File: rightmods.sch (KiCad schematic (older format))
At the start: 22 parts

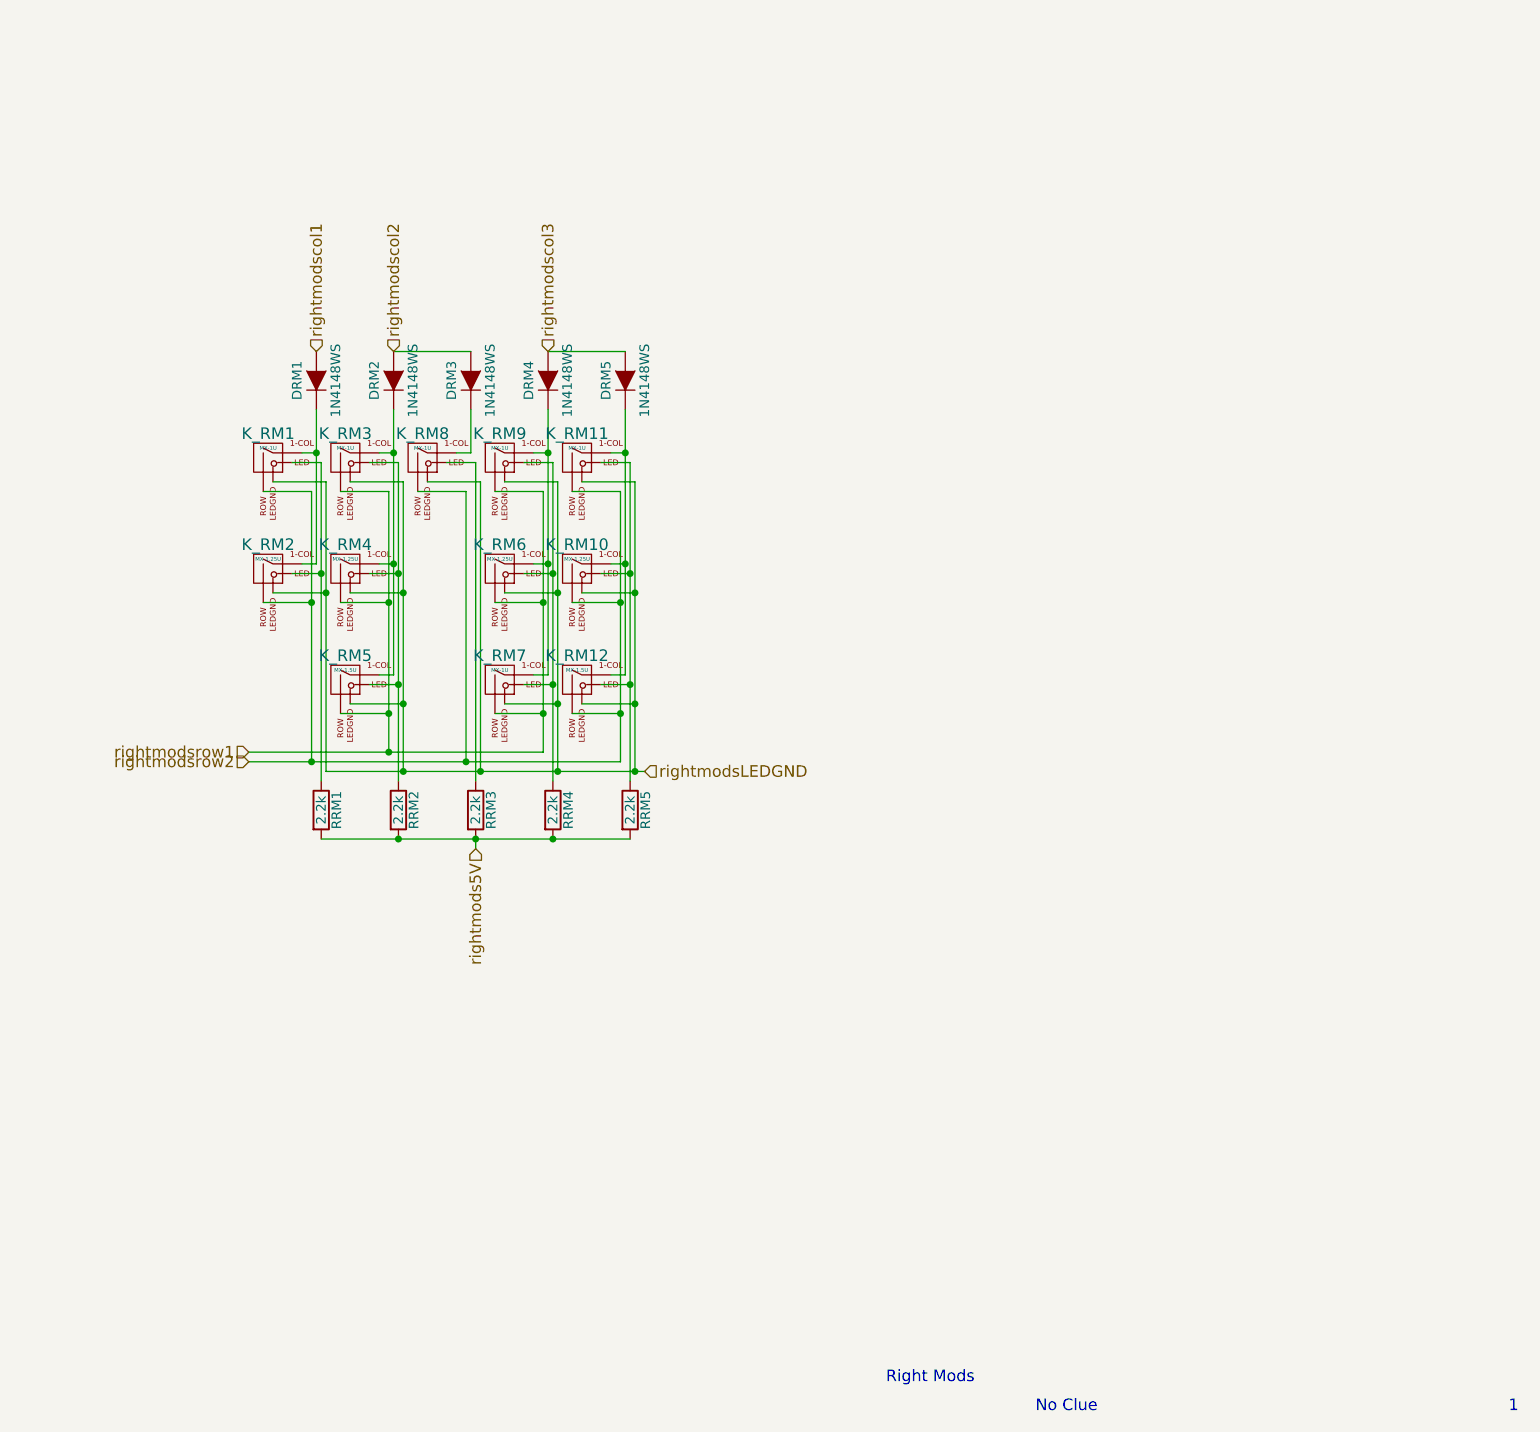
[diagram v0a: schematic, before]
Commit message: Added more right shift layouts
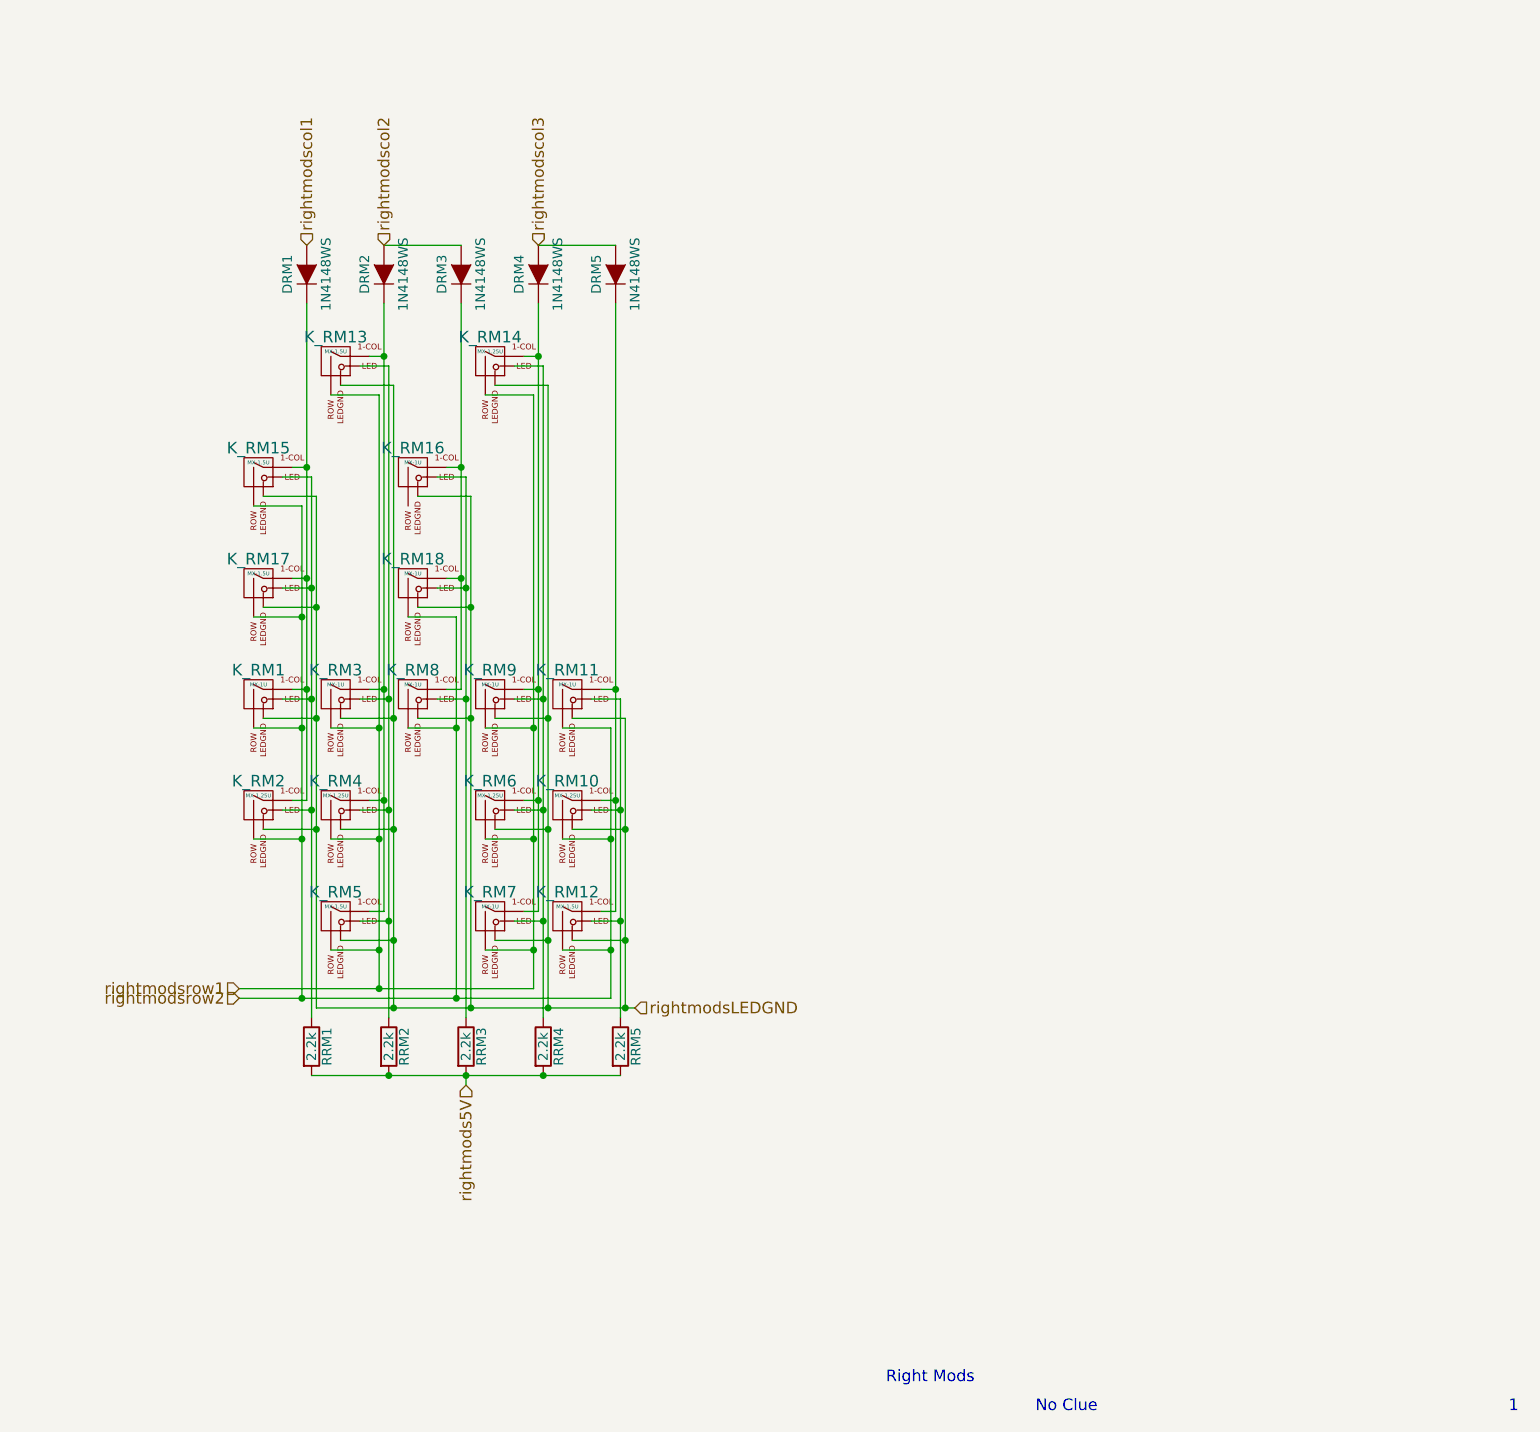
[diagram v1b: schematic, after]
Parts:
- added K_RM13, K_RM15, K_RM17: MX-1.5U, MX_Alps_Hybrid:MX-1.5U, symbol MX-1.5U
- added K_RM14: MX-1.25U, MX_Alps_Hybrid:MX-1.25U, symbol MX-1.25U
- added K_RM16, K_RM18: MX-1U, MX_Alps_Hybrid:MX-1U, symbol MX-1U
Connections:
- net rightmodsLEDGND: now also K_RM13.4 (LEDGND), K_RM14.4 (LEDGND), K_RM15.4 (LEDGND), K_RM16.4 (LEDGND), K_RM17.4 (LEDGND), K_RM18.4 (LEDGND)
- net rightmodsrow1: now also K_RM13.2 (ROW), K_RM14.2 (ROW)
- net rightmodsrow2: now also K_RM15.2 (ROW), K_RM17.2 (ROW), K_RM18.2 (ROW)
- net at DRM1.1 (K), K_RM1.1 (COL), K_RM2.1 (COL): now also K_RM15.1 (COL), K_RM17.1 (COL)
- net at K_RM1.3 (LED), K_RM2.3 (LED), RRM1.1: now also K_RM15.3 (LED), K_RM17.3 (LED)
- net at DRM2.1 (K), K_RM3.1 (COL), K_RM4.1 (COL)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: now also K_RM13.1 (COL)
- net at K_RM3.3 (LED), K_RM4.3 (LED), K_RM5.3 (LED)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: now also K_RM13.3 (LED)
- net at DRM4.1 (K), K_RM6.1 (COL), K_RM7.1 (COL)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: now also K_RM14.1 (COL)
- net at K_RM6.3 (LED), K_RM7.3 (LED), K_RM9.3 (LED)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: now also K_RM14.3 (LED)
- net at DRM3.1 (K), K_RM8.1 (COL): now also K_RM16.1 (COL), K_RM18.1 (COL)
- net at K_RM8.3 (LED), RRM3.1: now also K_RM16.3 (LED), K_RM18.3 (LED)
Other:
- moved on the sheet: DRM1, DRM2, DRM3, DRM4, DRM5, K_RM1, K_RM10, K_RM11, K_RM12, K_RM2, K_RM3, K_RM4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

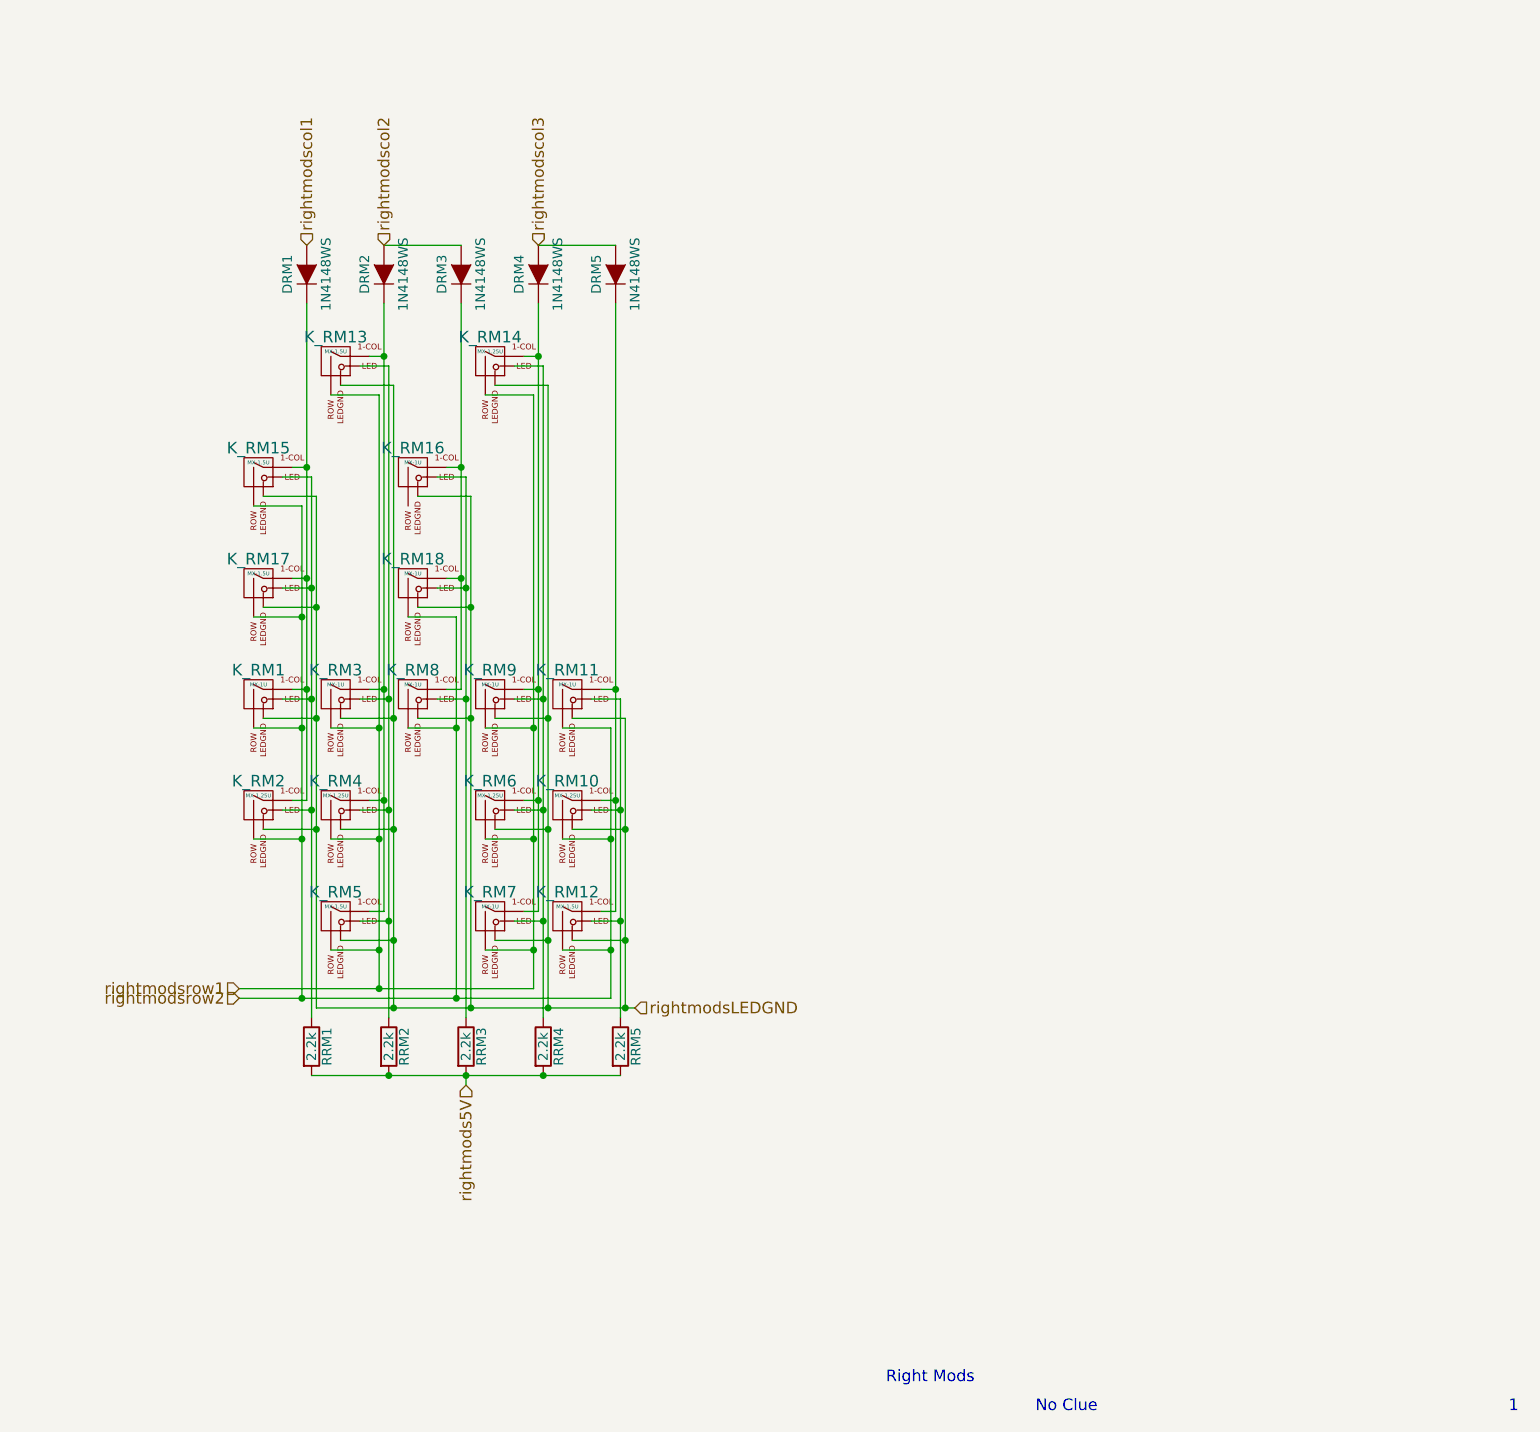
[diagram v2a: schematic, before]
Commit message: Fix RMods Diode Location
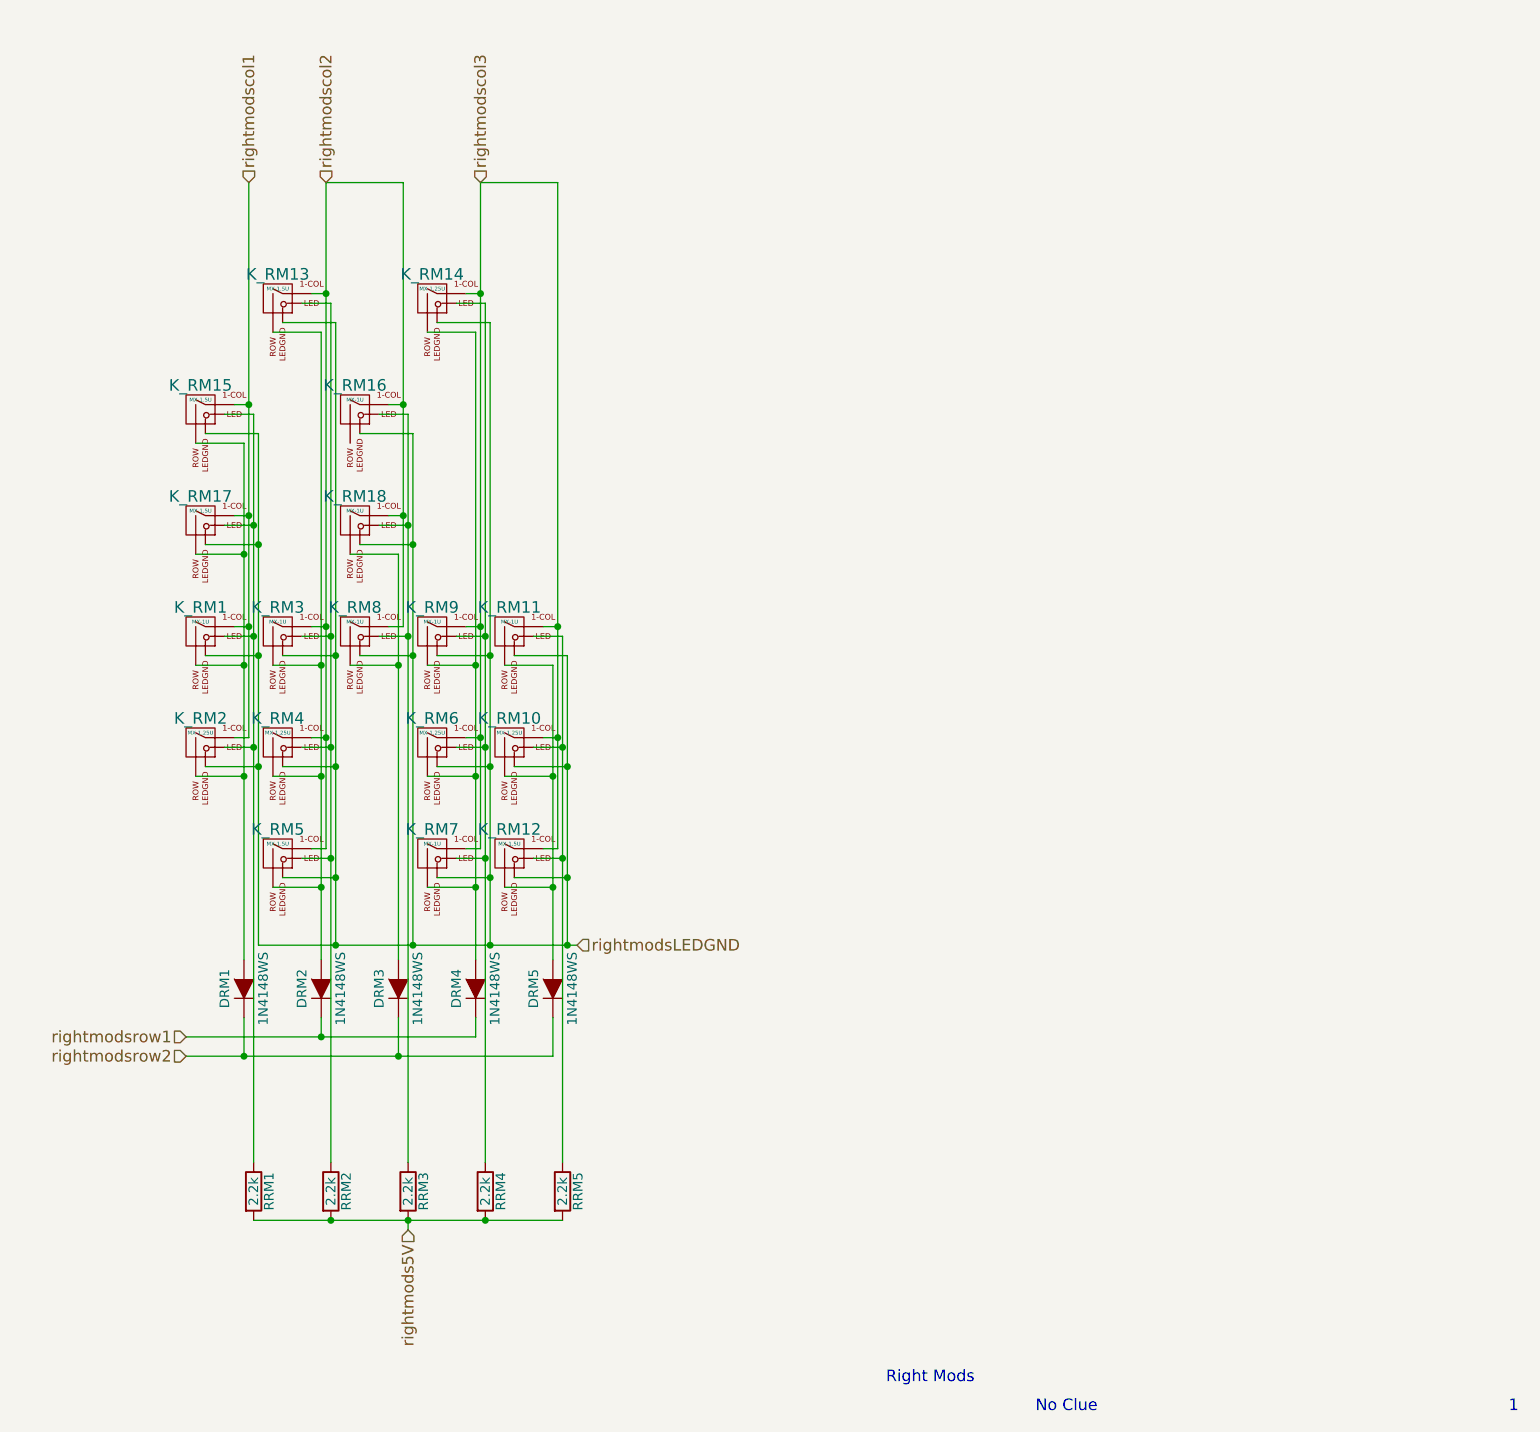
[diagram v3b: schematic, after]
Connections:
- net rightmodscol1: now also K_RM1.1 (COL), K_RM15.1 (COL), K_RM17.1 (COL), K_RM2.1 (COL); no longer DRM1.2 (A)
- net rightmodscol2: now also K_RM13.1 (COL), K_RM16.1 (COL), K_RM18.1 (COL), K_RM3.1 (COL), K_RM4.1 (COL), K_RM5.1 (COL), K_RM8.1 (COL); no longer DRM2.2 (A), DRM3.2 (A)
- net rightmodscol3: now also K_RM10.1 (COL), K_RM11.1 (COL), K_RM12.1 (COL), K_RM14.1 (COL), K_RM6.1 (COL), K_RM7.1 (COL), K_RM9.1 (COL); no longer DRM4.2 (A), DRM5.2 (A)
- net rightmodsrow1: now also DRM2.1 (K), DRM4.1 (K); no longer K_RM13.2 (ROW), K_RM14.2 (ROW), K_RM3.2 (ROW), K_RM4.2 (ROW), K_RM5.2 (ROW), K_RM6.2 (ROW), K_RM7.2 (ROW), K_RM9.2 (ROW)
- net rightmodsrow2: now also DRM1.1 (K), DRM3.1 (K), DRM5.1 (K); no longer K_RM1.2 (ROW), K_RM10.2 (ROW), K_RM11.2 (ROW), K_RM12.2 (ROW), K_RM15.2 (ROW), K_RM17.2 (ROW), K_RM18.2 (ROW), K_RM2.2 (ROW), K_RM8.2 (ROW)
- new net: DRM1.2 (A), K_RM1.2 (ROW), K_RM15.2 (ROW), K_RM17.2 (ROW), K_RM2.2 (ROW)
- new net: DRM2.2 (A), K_RM13.2 (ROW), K_RM3.2 (ROW), K_RM4.2 (ROW), K_RM5.2 (ROW)
- new net: DRM4.2 (A), K_RM14.2 (ROW), K_RM6.2 (ROW), K_RM7.2 (ROW), K_RM9.2 (ROW)
- new net: DRM3.2 (A), K_RM18.2 (ROW), K_RM8.2 (ROW)
- new net: DRM5.2 (A), K_RM10.2 (ROW), K_RM11.2 (ROW), K_RM12.2 (ROW)
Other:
- moved on the sheet: DRM1, DRM2, DRM3, DRM4, DRM5, K_RM1, K_RM10, K_RM11, K_RM12, K_RM13, K_RM14, K_RM15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
